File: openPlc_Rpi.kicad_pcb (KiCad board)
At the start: 2 copper layers, 155 x 108 mm, 104 parts, among them J1 Raspberry_Pi_2_3, J10 Conn_01x04, J11 Conn_01x04, J12 Conn_01x04, J13 Conn_01x04, J2 Screw_Terminal_01x05, J3 Screw_Terminal_01x04, J4 Screw_Terminal_01x02, J5 Screw_Terminal_01x12, J6 Screw_Terminal_01x05, J7 Screw_Terminal_01x12, J8 Screw_Terminal_01x02, J9 Screw_Terminal_01x02, K1 G5LE-1, K2 G5LE-1, K3 G5LE-1, K4 G5LE-1, K5 G5LE-1, K6 G5LE-1, K7 G5LE-1, K8 G5LE-1, Q1 BSS123, U1 power_LM2576, U2 LTV-847, U3 LTV-847, U4 power_L7812_smd, U5 MAX481E, U6 ADS1018IDGS, U7 AMS1117-3.3, U8 ULN2803A

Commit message: [vishnu] unknown
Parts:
- removed J2, J6: Screw_Terminal_01x05, TerminalBlocks_Phoenix:TerminalBlock_Phoenix_MKDS1.5-5pol
- added D20: LED, LED_SMD:LED_0805_2012Metric_Pad1.15x1.40mm_HandSolder, F.Cu at (78.2, 82.0)
- added D21: LED, LED_SMD:LED_0805_2012Metric_Pad1.15x1.40mm_HandSolder, F.Cu at (183.8, 81.7)
- added D22: LED, LED_SMD:LED_0805_2012Metric_Pad1.15x1.40mm_HandSolder, F.Cu at (175.6, 81.9)
- added J14: Screw_Terminal_01x10, TerminalBlock_Phoenix:TerminalBlock_Phoenix_MKDS-1,5-10-5.08_1x10_P5.08mm_Horizontal, F.Cu at (131.2, 53.1)
- added Q2: 2N7002, Package_TO_SOT_SMD:SOT-23, F.Cu at (179.5, 81.7)
- added Q3: 2N7002, Package_TO_SOT_SMD:SOT-23, F.Cu at (171.4, 81.9)
- added R46: 220R, Resistor_SMD:R_0805_2012Metric_Pad1.15x1.40mm_HandSolder, F.Cu at (73.2, 82.0)
- added R47: 510R, Resistor_SMD:R_0805_2012Metric_Pad1.15x1.40mm_HandSolder, F.Cu at (179.5, 78.7)
- added R48: 510R, Resistor_SMD:R_0805_2012Metric_Pad1.15x1.40mm_HandSolder, F.Cu at (171.4, 78.7)
- C1, C4, C8: footprint Capacitors_SMD:C_0805_HandSoldering -> Capacitor_SMD:C_0805_2012Metric_Pad1.15x1.40mm_HandSolder
- C2: footprint Capacitors_SMD:CP_Elec_8x10 -> Capacitor_SMD:CP_Elec_8x10
- C3: footprint Capacitors_SMD:CP_Elec_10x10 -> Capacitor_SMD:CP_Elec_10x10
- C5, C6: value C -> 22uf; footprint Capacitors_SMD:C_0805_HandSoldering -> Capacitor_SMD:C_0805_2012Metric_Pad1.15x1.40mm_HandSolder
- C7: value Cap_tantalum_1206_3218 -> .33uf
- C9: value C -> 1uf; footprint Capacitors_SMD:C_0805_HandSoldering -> Capacitor_SMD:C_0805_2012Metric_Pad1.15x1.40mm_HandSolder
- D5: value D_Zener -> NTS245SF
- D6: value D_Schottky_power -> B340
- J3: footprint TerminalBlocks_Phoenix:TerminalBlock_Phoenix_MKDS1.5-4pol -> TerminalBlock_Phoenix:TerminalBlock_Phoenix_MKDS-1,5-4-5.08_1x04_P5.08mm_Horizontal
- J4, J8, J9: footprint TerminalBlocks_Phoenix:TerminalBlock_Phoenix_MKDS1.5-2pol -> TerminalBlock_Phoenix:TerminalBlock_Phoenix_MKDS-1,5-2-5.08_1x02_P5.08mm_Horizontal
- J5, J7: footprint TerminalBlocks_Phoenix:TerminalBlock_Phoenix_MKDS1.5-12pol -> TerminalBlock_Phoenix:TerminalBlock_Phoenix_MKDS-1,5-12-5.08_1x12_P5.08mm_Horizontal
- R1, R10, R11, R12, R13, R14, R15, R16, R2, R21, R22, R23, R24, R25, R26, R27, R28, R3, R4, R41, R42, R43, R44, R45, R5, R6, R7, R8, R9: footprint Resistors_SMD:R_0805_HandSoldering -> Resistor_SMD:R_0805_2012Metric_Pad1.15x1.40mm_HandSolder
- R17, R18, R19, R20, R29, R30, R31, R32: value R -> 10k; footprint Resistors_SMD:R_0805_HandSoldering -> Resistor_SMD:R_0805_2012Metric_Pad1.15x1.40mm_HandSolder
- R33, R34, R35, R36, R37, R38, R39, R40: value R_US -> 220R; footprint Resistors_SMD:R_0805_HandSoldering -> Resistor_SMD:R_0805_2012Metric_Pad1.15x1.40mm_HandSolder
- moved D5 1.16 mm to (76.6, 60.8)
- moved J4 1.02 mm to (79.2, 53.1)
- moved J3 0.99 mm to (152.6, 53.0)
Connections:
- J1 pad 12: (no net) -> Net-(J1-Pad12)
- J1 pad 27: (no net) -> Net-(J1-Pad27)
- J1 pad 28: (no net) -> Net-(J1-Pad28)
- J1 pad 7: (no net) -> Net-(J1-Pad7)
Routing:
- net +3V3: track 156.1 -> 170.3 mm, vias 10 -> 12
- net GND: track 106.4 -> 119.7 mm, vias 0 -> 2
- net Net-(D22-Pad2): track 0.00 -> 6.85 mm
- net Net-(D21-Pad2): track 0.00 -> 6.74 mm
- net /RXD: track 64.6 -> 68.7 mm
- net +5V: track 523.6 -> 527.1 mm
- net Net-(D20-Pad2): track 0.00 -> 3.00 mm
- net +24V: track 270.8 -> 273.6 mm
- net /TXD: track 75.9 -> 77.9 mm
- net Net-(J3-Pad1): track 10.0 -> 10.7 mm
- net SDA: track 82.8 -> 83.4 mm
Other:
- board text added: "+24V"
- board text added: "A"
- board text added: "B"
- board text added: "GND"
- board text added: "POWER"
- board text added: "Relay 1"
- board text added: "Relay 2"
- board text added: "Relay 3"
- board text added: "Relay 4"
- board text added: "Relay 5"
- board text added: "Relay 6"
- board text added: "Relay 7"
- board text added: "Relay 8"
- board text added: "SCL"
- board text added: "SDA"

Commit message: [vishnu] created new standalone library for the project with all the necessary components and corresponding footprints.
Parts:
- C7: footprint Capacitors_SMD:C_1206_HandSoldering -> Capacitor_SMD:C_1206_3216Metric_Pad1.42x1.75mm_HandSolder
- D1, D10, D2, D3, D4, D7, D8, D9: footprint Diodes_SMD:D_1206 -> Diode_SMD:D_1206_3216Metric
- D11, D12, D13, D14, D15, D16, D17, D18: footprint LEDs:LED_0805_HandSoldering -> LED_SMD:LED_0805_2012Metric_Pad1.15x1.40mm_HandSolder
- D19: footprint Diodes_SMD:D_SMB_Handsoldering -> Diode_SMD:D_SMB_Handsoldering
- D5: footprint Diodes_SMD:D_SMA_Handsoldering -> Diode_SMD:D_SMA_Handsoldering
- D6: footprint Diodes_SMD:D_SMC_Handsoldering -> Diode_SMD:D_SMC_Handsoldering
- J1: footprint Socket_Strips:Socket_Strip_Straight_2x20_Pitch2.54mm -> openPlc_Rpi:Raspberry_Pi_Zero_Socketed_THT_FaceUp_SingleMountingHoles_copy
- J10, J11, J12, J13: footprint Connectors_JST:JST_XH_B04B-XH-A_04x2.50mm_Straight -> Connector_JST:JST_XH_B4B-XH-A_1x04_P2.50mm_Vertical
- K1, K2, K3, K4, K5, K6, K7, K8: footprint Relays_THT:Relay_SPDT_OMRON-G5LE-1 -> Relay_THT:Relay_SPDT_Omron-G5LE-1
- L1: footprint Inductors_SMD:L_12x12mm_h6mm -> Inductor_SMD:L_12x12mm_H6mm
- Q1: footprint TO_SOT_Packages_SMD:SOT-23 -> Package_TO_SOT_SMD:SOT-23
- U1: footprint TO_SOT_Packages_SMD:TO-263-5_TabPin3 -> Package_TO_SOT_SMD:TO-263-5_TabPin3
- U2, U3: footprint Housings_DIP:DIP-16_W7.62mm_SMDSocket_SmallPads -> Package_DIP:DIP-16_W8.89mm_SMDSocket_LongPads
- U4: footprint TO_SOT_Packages_SMD:TO-263-2 -> Package_TO_SOT_SMD:TO-263-2
- U5: footprint Housings_SOIC:SOIC-8_3.9x4.9mm_Pitch1.27mm -> Package_SO:SOIC-8_3.9x4.9mm_P1.27mm
- U6: footprint Housings_SSOP:TSSOP-10_3x3mm_Pitch0.5mm -> Package_SO:TSSOP-10_3x3mm_P0.5mm
- U7: footprint TO_SOT_Packages_SMD:SOT-223-3_TabPin2 -> Package_TO_SOT_SMD:SOT-223-3_TabPin2
- U8: footprint Housings_SOIC:SOIC-18W_7.5x11.6mm_Pitch1.27mm -> Package_SO:SOIC-18W_7.5x11.6mm_P1.27mm
- moved J1 3.10 mm to (136.9, 98.8)
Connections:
- J1 pad 11: DO_7 -> DI_7
- J1 pad 13: DO_6 -> DI_6
- J1 pad 15: DO_5 -> DI_5
- J1 pad 16: DI_7 -> DO_7
- J1 pad 18: DI_6 -> DO_6
- J1 pad 22: DI_5 -> DO_5
- J1 pad 26: DI_4 -> DO_4
- J1 pad 29: DO_4 -> DI_4
- J1 pad 31: DO_3 -> DI_3
- J1 pad 32: DI_3 -> DO_3
- J1 pad 33: DO_2 -> DI_2
- J1 pad 35: DO_1 -> DI_1
- J1 pad 36: DI_2 -> DO_2
- J1 pad 37: DO_0 -> DI_0
- J1 pad 38: DI_1 -> DO_1
- J1 pad 40: DI_0 -> DO_0
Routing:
- net SCL: track 77.2 -> 86.1 mm
- net GND: track 119.7 -> 110.7 mm

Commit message: [vishnu] replaced Rpi symbol and footprint in schematic and pcb from the new library
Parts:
- J1: footprint openPlc_Rpi:Raspberry_Pi_Zero_Socketed_THT_FaceUp_SingleMountingHoles_copy -> fossee_openplc:Raspberry_Pi_Zero_FaceUp_SingleMountingHole
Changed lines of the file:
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@@
     (add_net /9)
   )
-  (module openPlc_Rpi:Raspberry_Pi_Zero_Socketed_THT_FaceUp_SingleMountingHoles_copy (layer F.Cu)
+  (module fossee_openplc:Raspberry_Pi_Zero_FaceUp_SingleMountingHole (layer F.Cu)
     (at 136.8806 98.7552 270)
     (descr "Raspberry Pi Zero using through hole straight pin socket, 2x20, 2.54mm pitch, https://www.raspberrypi.org/documentation/hardware/raspberrypi/mechanical/rpi_MECH_Zero_1p2.pdf")

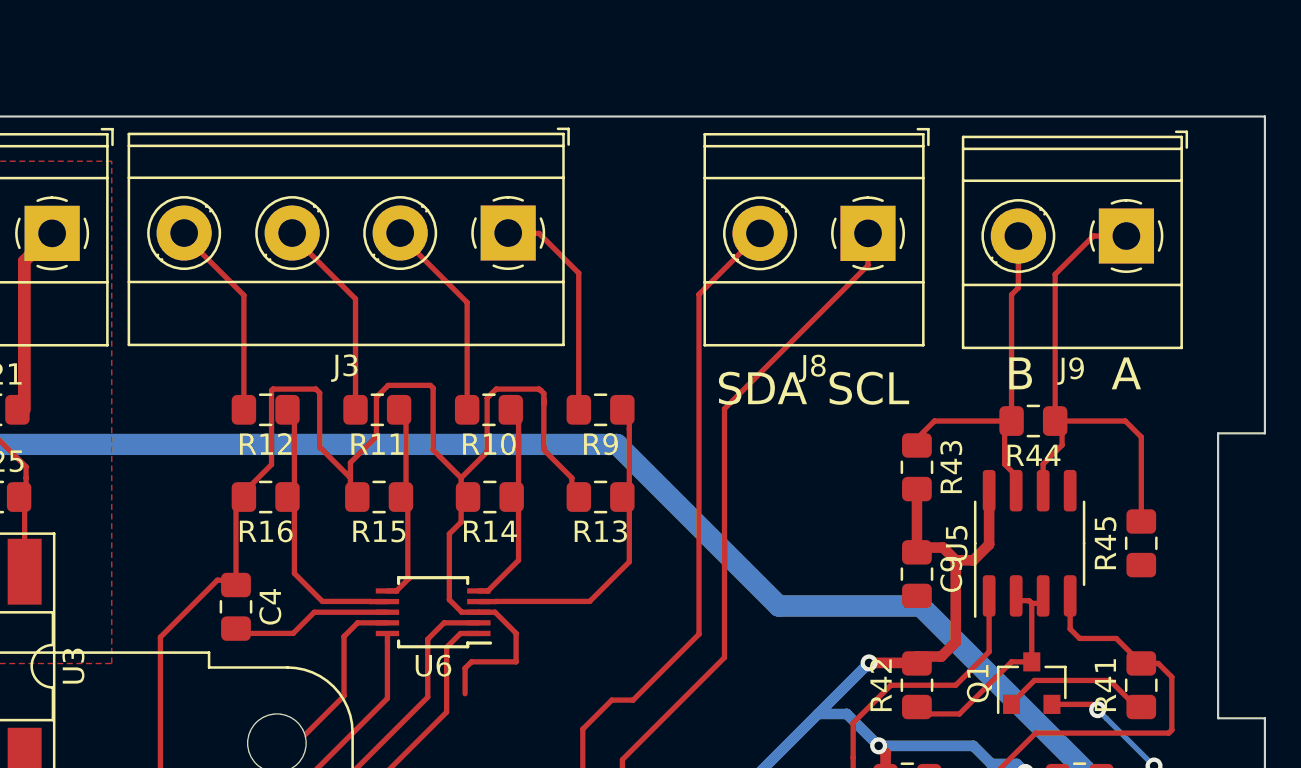
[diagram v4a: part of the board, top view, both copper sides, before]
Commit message: [vishnu] replaced ADC circuit with new library components : scehmatic and PCB updated
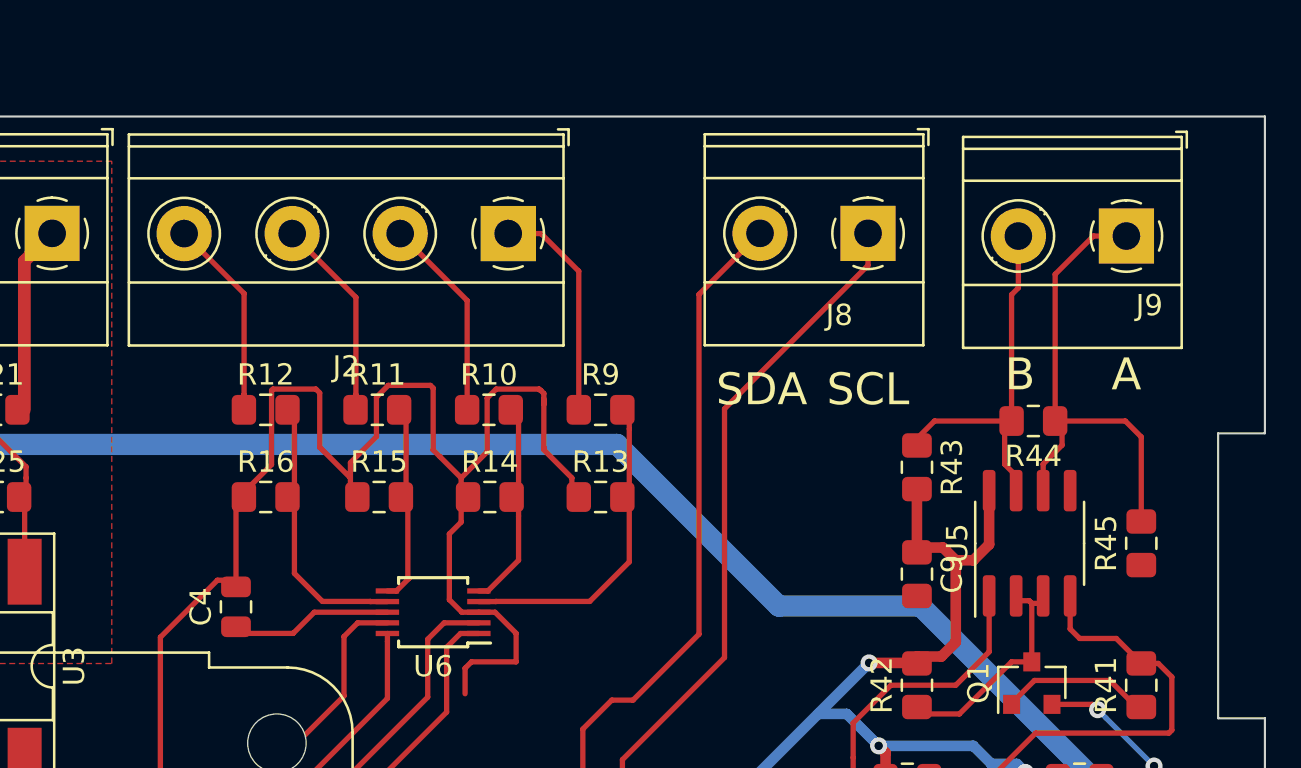
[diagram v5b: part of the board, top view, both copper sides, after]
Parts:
- removed J3: Screw_Terminal_01x04, TerminalBlock_Phoenix:TerminalBlock_Phoenix_MKDS-1,5-4-5.08_1x04_P5.08mm_Horizontal
- added J2: Screw_Terminal_01x04, fossee_openplc:TerminalBlock_Phoenix_MKDS-1,5-4-5.08_1x04_P5.08mm_Horizontal, F.Cu at (152.6, 53.1)
- C4: footprint Capacitor_SMD:C_0805_2012Metric_Pad1.15x1.40mm_HandSolder -> fossee_openplc:C_0805_2012Metric
- R10, R11, R12, R13, R14, R15, R16, R9: footprint Resistor_SMD:R_0805_2012Metric_Pad1.15x1.40mm_HandSolder -> fossee_openplc:R_0805_2012Metric_Pad1.15x1.40mm_HandSolder
- U6: footprint Package_SO:TSSOP-10_3x3mm_P0.5mm -> fossee_openplc:TSSOP-10_3x3mm_P0.5mm
- turned C4 to 90 degrees
- turned R10 to 0 degrees
- turned R11 to 0 degrees
- turned R12 to 0 degrees
- turned R13 to 0 degrees
- turned R14 to 0 degrees
- turned R15 to 0 degrees
- turned R16 to 0 degrees
- turned R9 to 0 degrees
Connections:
- C4 pad 1: GND -> Net-(C4-Pad1)
- C4 pad 2: Net-(C4-Pad2) -> GND
- R10 pad 1: Net-(R10-Pad1) -> Net-(J2-Pad2)
- R10 pad 2: Net-(J3-Pad2) -> Net-(R10-Pad2)
- R11 pad 1: Net-(R11-Pad1) -> Net-(J2-Pad3)
- R11 pad 2: Net-(J3-Pad3) -> Net-(R11-Pad2)
- R12 pad 1: Net-(R12-Pad1) -> Net-(J2-Pad4)
- R12 pad 2: Net-(J3-Pad4) -> Net-(R12-Pad2)
- R13 pad 1: Net-(R13-Pad1) -> GND
- R13 pad 2: GND -> Net-(R13-Pad2)
- R14 pad 1: Net-(R10-Pad1) -> GND
- R14 pad 2: GND -> Net-(R10-Pad2)
- R15 pad 1: Net-(R11-Pad1) -> GND
- R15 pad 2: GND -> Net-(R11-Pad2)
- R16 pad 1: Net-(R12-Pad1) -> GND
- R16 pad 2: GND -> Net-(R12-Pad2)
- R9 pad 1: Net-(R13-Pad1) -> Net-(J2-Pad1)
- R9 pad 2: Net-(J3-Pad1) -> Net-(R13-Pad2)
- U6 pad 4: Net-(R13-Pad1) -> Net-(R13-Pad2)
- U6 pad 5: Net-(R10-Pad1) -> Net-(R10-Pad2)
- U6 pad 6: Net-(R11-Pad1) -> Net-(R11-Pad2)
- U6 pad 7: Net-(R12-Pad1) -> Net-(R12-Pad2)
- U6 pad 8: Net-(C4-Pad2) -> Net-(C4-Pad1)
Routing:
- net Net-(R13-Pad2): track 0.00 -> 15.0 mm
- net Net-(R13-Pad1): track 15.0 -> 0.00 mm
- net Net-(R12-Pad2): track 0.00 -> 12.6 mm
- net Net-(R12-Pad1): track 12.6 -> 0.00 mm
- net Net-(J3-Pad1): track 10.7 -> 0.00 mm
- net Net-(J2-Pad1): track 0.00 -> 10.6 mm
- net Net-(J3-Pad2): track 9.64 -> 0.00 mm
- net Net-(J2-Pad2): track 0.00 -> 9.59 mm
- net Net-(J3-Pad3): track 9.57 -> 0.00 mm
- net Net-(R10-Pad2): track 0.00 -> 9.56 mm
- net Net-(R10-Pad1): track 9.56 -> 0.00 mm
- net Net-(J2-Pad3): track 0.00 -> 9.54 mm
- net Net-(J3-Pad4): track 9.50 -> 0.00 mm
- net Net-(J2-Pad4): track 0.00 -> 9.46 mm
- net Net-(R11-Pad2): track 0.00 -> 9.24 mm
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
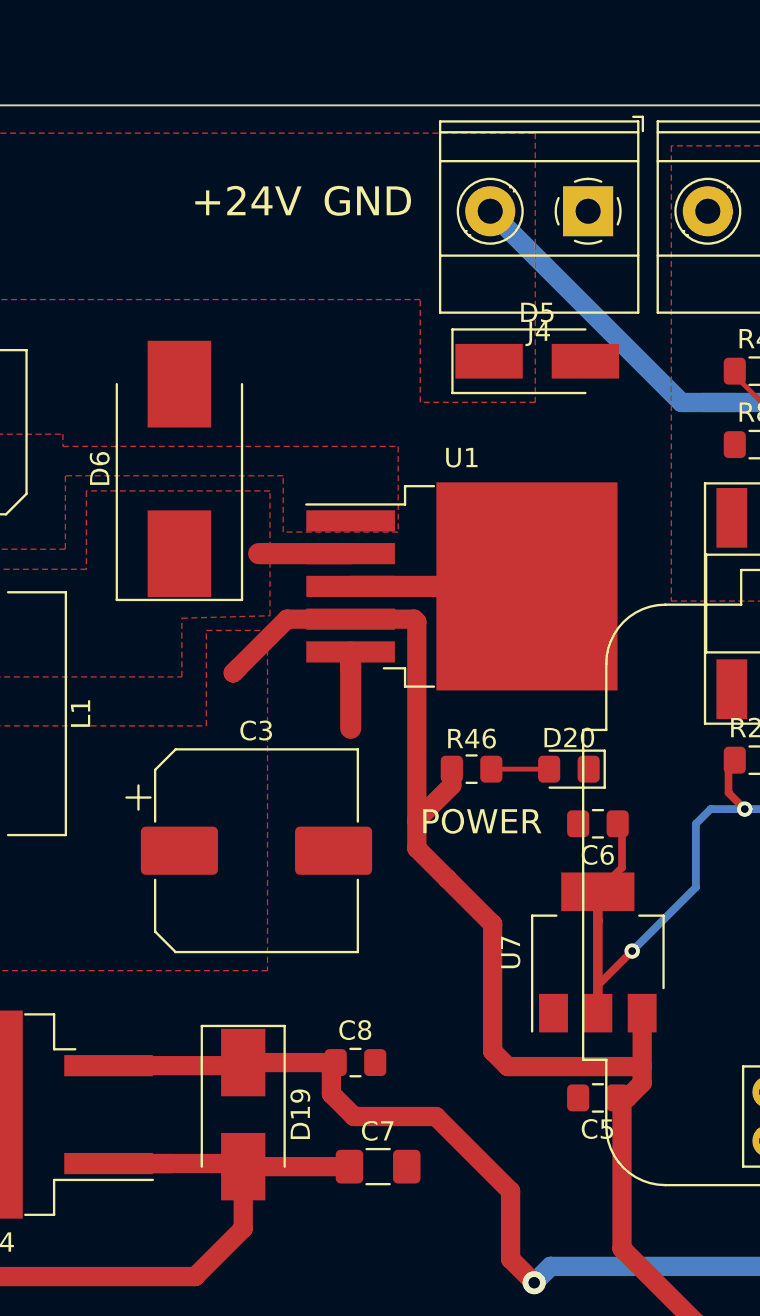
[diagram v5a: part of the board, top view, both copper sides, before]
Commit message: [vishnu] Replaced all component in the POWER circuitry with local library components. Added tantalum, C_1206, AMS117 and ls812 parts to the library.
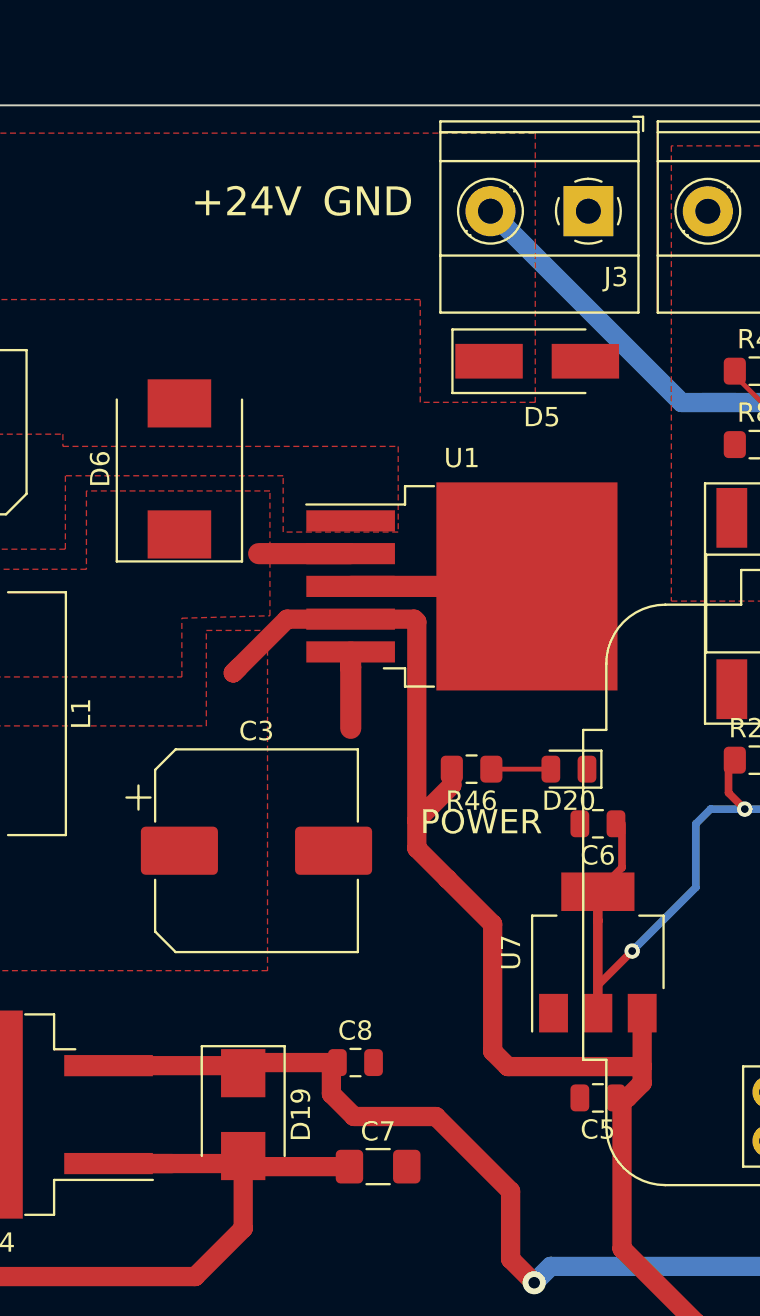
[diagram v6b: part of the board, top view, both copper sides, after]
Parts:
- removed J4: Screw_Terminal_01x02, TerminalBlock_Phoenix:TerminalBlock_Phoenix_MKDS-1,5-2-5.08_1x02_P5.08mm_Horizontal
- added J3: Screw_Terminal_01x02, fossee_openplc:TerminalBlock_Phoenix_MKDS-1,5-2-5.08_1x02_P5.08mm_Horizontal, F.Cu at (79.3, 53.0)
- C2: footprint Capacitor_SMD:CP_Elec_8x10 -> fossee_openplc:CP_Elec_8x10
- C3: footprint Capacitor_SMD:CP_Elec_10x10 -> fossee_openplc:CP_Elec_10x10
- C5, C6, C8: footprint Capacitor_SMD:C_0805_2012Metric_Pad1.15x1.40mm_HandSolder -> fossee_openplc:C_0805_2012Metric
- C7: footprint Capacitor_SMD:C_1206_3216Metric_Pad1.42x1.75mm_HandSolder -> fossee_openplc:C_1206_3216Metric_Pad1.42x1.75mm_HandSolder
- D19: footprint Diode_SMD:D_SMB_Handsoldering -> fossee_openplc:D_SMB
- D20: value LED -> LED_ALT; footprint LED_SMD:LED_0805_2012Metric_Pad1.15x1.40mm_HandSolder -> fossee_openplc:LED_0805_2012Metric
- D5: footprint Diode_SMD:D_SMA_Handsoldering -> fossee_openplc:D_SMA_Handsoldering
- D6: footprint Diode_SMD:D_SMC_Handsoldering -> fossee_openplc:D_SMC
- J10, J11, J13: footprint Connector_JST:JST_XH_B4B-XH-A_1x04_P2.50mm_Vertical -> fossee_openplc:JST_XH_B4B-XH-A_1x04_P2.50mm_Vertical
- L1: footprint Inductor_SMD:L_12x12mm_H6mm -> fossee_openplc:L_12x12mm_H6mm
- R46: value 220R -> 220; footprint Resistor_SMD:R_0805_2012Metric_Pad1.15x1.40mm_HandSolder -> fossee_openplc:R_0805_2012Metric_Pad1.15x1.40mm_HandSolder
- U1: footprint Package_TO_SOT_SMD:TO-263-5_TabPin3 -> fossee_openplc:TO-263-5_TabPin3
- U4: footprint Package_TO_SOT_SMD:TO-263-2 -> fossee_openplc:TO-263-2
- U7: footprint Package_TO_SOT_SMD:SOT-223-3_TabPin2 -> fossee_openplc:SOT-223-3_TabPin2
- turned R46 to 180 degrees
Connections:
- R46 pad 1: +5V -> Net-(D20-Pad2)
- R46 pad 2: Net-(D20-Pad2) -> +5V

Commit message: [vishnu] Replaced all components in the OUTPUT circuit with local library "fossee_openplc" parts. Deleted an outdated folder with SVG of the older version of the PCB.
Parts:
- C1: footprint Capacitor_SMD:C_0805_2012Metric_Pad1.15x1.40mm_HandSolder -> fossee_openplc:C_0805_2012Metric
- D1, D10, D2, D3, D4, D7, D8, D9: footprint Diode_SMD:D_1206_3216Metric -> fossee_openplc:D_1206_3216Metric
- D11, D12, D13, D14, D15, D16, D17, D18: footprint LED_SMD:LED_0805_2012Metric_Pad1.15x1.40mm_HandSolder -> fossee_openplc:LED_0805_2012Metric
- J5, J7: footprint TerminalBlock_Phoenix:TerminalBlock_Phoenix_MKDS-1,5-12-5.08_1x12_P5.08mm_Horizontal -> fossee_openplc:TerminalBlock_Phoenix_MKDS-1,5-12-5.08_1x12_P5.08mm_Horizontal
- K1, K2, K3, K4, K5, K6, K7, K8: footprint Relay_THT:Relay_SPDT_Omron-G5LE-1 -> fossee_openplc:Relay_SPDT_Omron-G5LE-1
- R33, R34, R35, R36, R37, R38, R39, R40: footprint Resistor_SMD:R_0805_2012Metric_Pad1.15x1.40mm_HandSolder -> fossee_openplc:R_0805_2012Metric_Pad1.15x1.40mm_HandSolder
- U8: footprint Package_SO:SOIC-18W_7.5x11.6mm_P1.27mm -> fossee_openplc:SOIC-18W_7.5x11.6mm_P1.27mm
- turned R33 to 180 degrees
- turned R34 to 180 degrees
- turned R35 to 180 degrees
- turned R36 to 180 degrees
- turned R37 to 180 degrees
- turned R38 to 180 degrees
- turned R39 to 180 degrees
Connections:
- R33 pad 1: +5V -> Net-(D11-Pad2)
- R33 pad 2: Net-(D11-Pad2) -> +5V
- R34 pad 1: +5V -> Net-(D12-Pad2)
- R34 pad 2: Net-(D12-Pad2) -> +5V
- R35 pad 1: +5V -> Net-(D13-Pad2)
- R35 pad 2: Net-(D13-Pad2) -> +5V
- R36 pad 1: +5V -> Net-(D14-Pad2)
- R36 pad 2: Net-(D14-Pad2) -> +5V
- R37 pad 1: +5V -> Net-(D15-Pad2)
- R37 pad 2: Net-(D15-Pad2) -> +5V
- R38 pad 1: +5V -> Net-(D16-Pad2)
- R38 pad 2: Net-(D16-Pad2) -> +5V
- R39 pad 1: +5V -> Net-(D17-Pad2)
- R39 pad 2: Net-(D17-Pad2) -> +5V
